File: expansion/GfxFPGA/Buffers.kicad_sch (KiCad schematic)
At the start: 20 parts, among them U201 SN74LVC8T245PWR, U202 SN74LVC8T245PWR, U203 SN74LVC8T245PWR, U204 SN74LVC8T245PWR, U205 SN74LVC8T245PWR, U206 SN74LVC8T245PWR

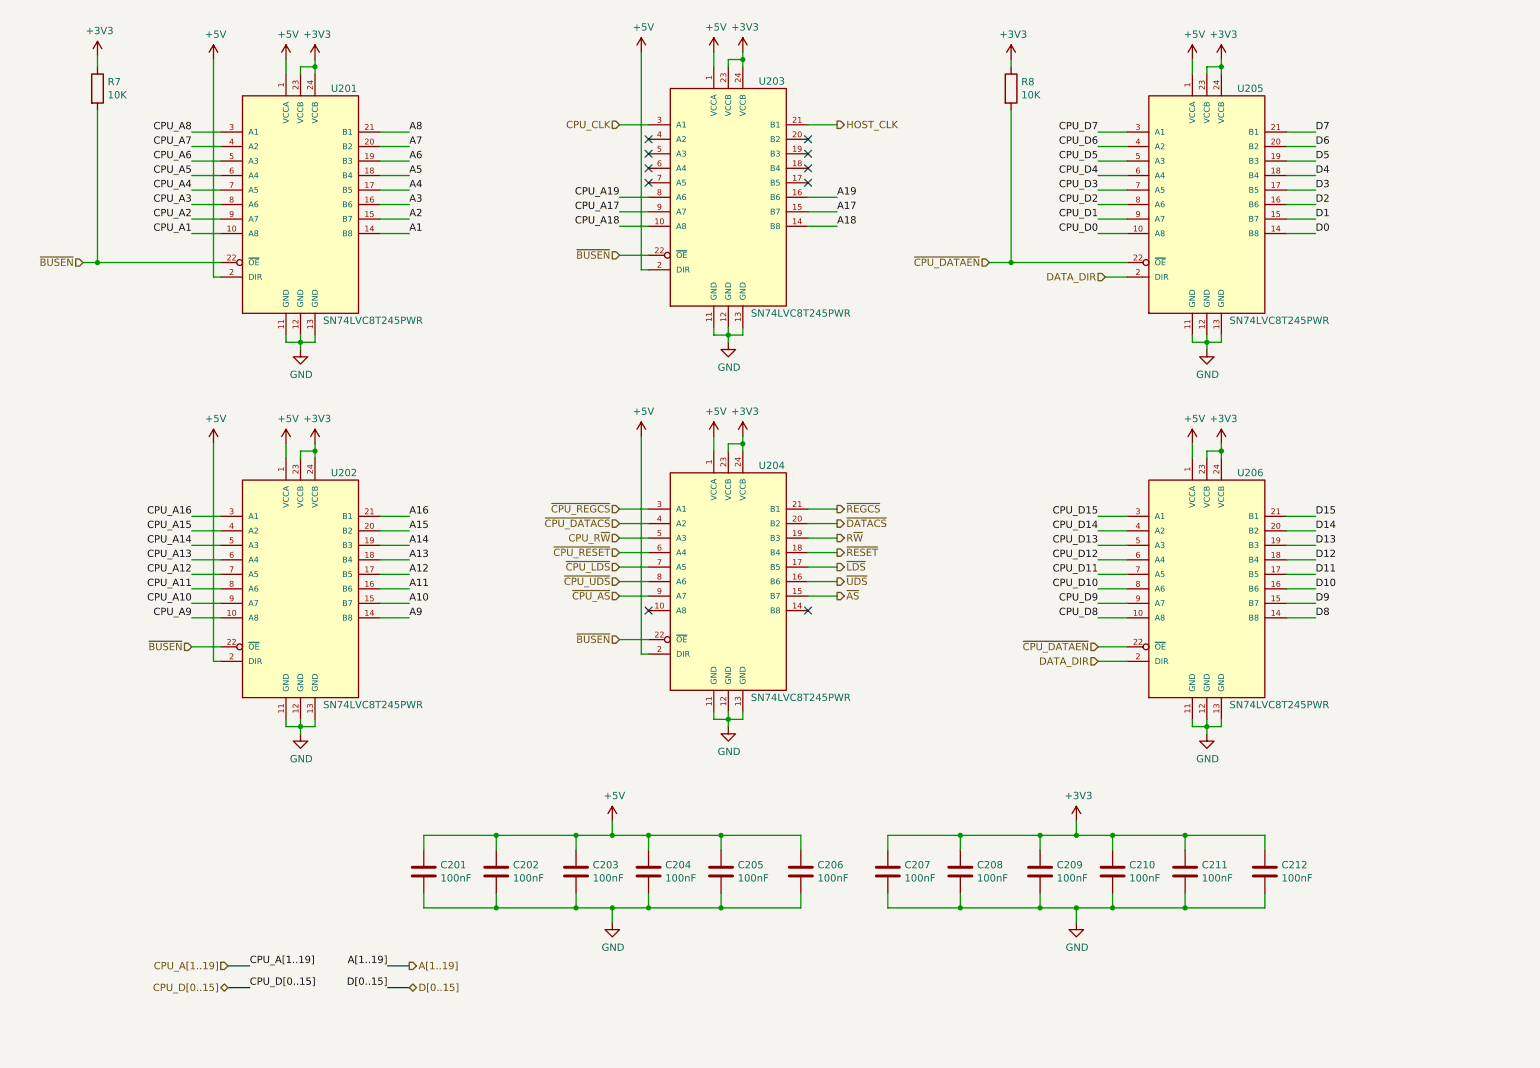
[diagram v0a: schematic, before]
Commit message: WOrking on FPGA VGA board
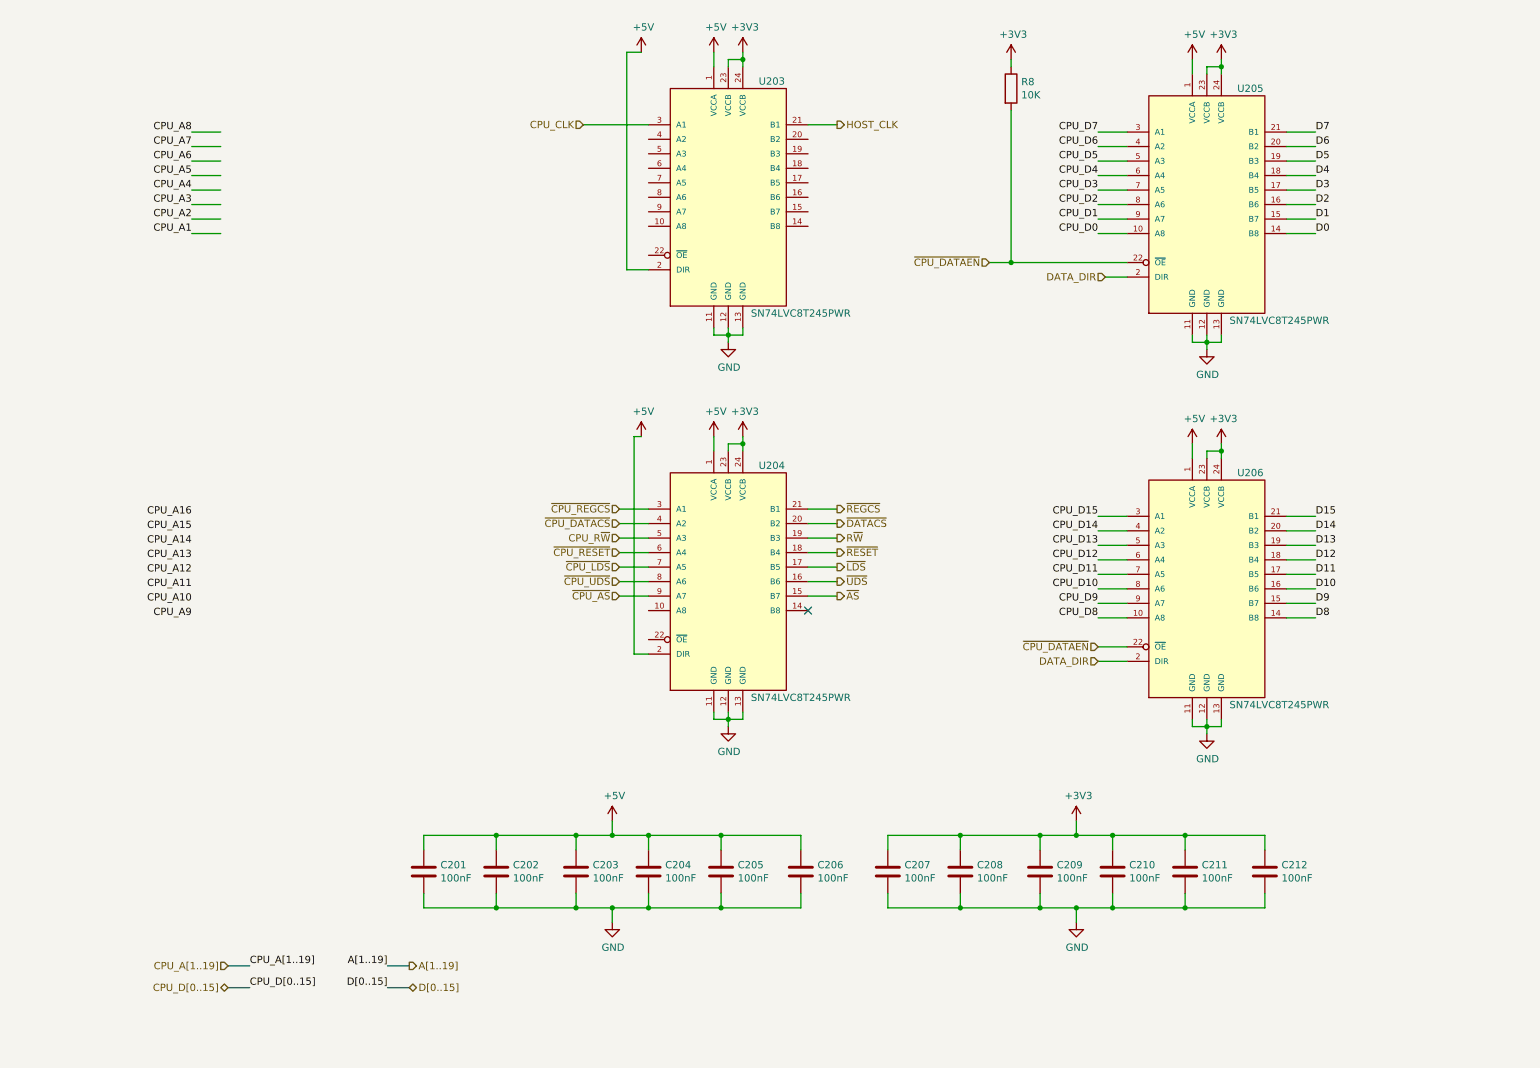
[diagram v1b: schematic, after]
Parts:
- removed R7: 10K, Resistor_SMD:R_0805_2012Metric, symbol Device:R
- removed U201, U202: SN74LVC8T245PWR, Ddraig:SOP65P640X120-24N, symbol Ddraig:SN74LVC8T245PWR
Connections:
- net A17: no longer names the net of U203.15 (B7)
- net A18: no longer names the net of U203.14 (B8)
- net A19: no longer names the net of U203.16 (B6)
- net CPU_A17: no longer names the net of U203.9 (A7)
- net CPU_A18: no longer names the net of U203.10 (A8)
- net CPU_A19: no longer names the net of U203.8 (A6)
- net ~{BUSEN}: no longer names the net of U203.22 (~{OE})
- net ~{BUSEN}: no longer U204.22 (~{OE})
- no-connect marks 10 -> 1

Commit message: WOrking on VGA card
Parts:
- removed C212: 100nF, Capacitor_SMD:C_0805_2012Metric, symbol Device:C
- added C25: 100nF, Capacitor_SMD:C_0805_2012Metric, symbol Device:C
- added U5, U6, U7: SN74LS157NSR, Package_SO:SO-16_5.3x10.2mm_P1.27mm, symbol 74xx:74LS157
- added U8: SN74LV1T34DBV, Package_TO_SOT_SMD:SOT-23-5, symbol Logic_LevelTranslator:SN74LV1T34DBV
- renumbered C208 to C21, C209 to C22, C210 to C23, C211 to C24, C201 to C26, C202 to C27, C203 to C28, C204 to C29, C205 to C30, C206 to C31, C207 to C32, R8 to R20, U204 to U10, U205 to U11, U206 to U12, U203 to U9
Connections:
- net +3V3: now also C25.1, U8.5 (VCC); no longer C32.1
- net +5V: now also C32.1, U5.16 (VCC), U6.16 (VCC), U7.16 (VCC)
- net CPU_A1: now also U5.2 (I0a)
- net CPU_A10: now also U6.5 (I0b)
- net CPU_A11: now also U5.3 (I1a)
- net CPU_A12: now also U5.6 (I1b)
- net CPU_A13: now also U5.10 (I1c)
- net CPU_A14: now also U5.13 (I1d)
- net CPU_A15: now also U7.3 (I1a)
- net CPU_A16: now also U7.6 (I1b)
- net CPU_A2: now also U5.5 (I0b)
- net CPU_A3: now also U5.11 (I0c)
- net CPU_A4: now also U5.14 (I0d)
- net CPU_A5: now also U7.2 (I0a)
- net CPU_A6: now also U7.5 (I0b)
- net CPU_A7: now also U7.11 (I0c)
- net CPU_A8: now also U7.14 (I0d)
- net CPU_A9: now also U6.2 (I0a)
- net CPU_D0: now also U11.3 (A1); no longer U11.10 (A8)
- net CPU_D1: now also U11.4 (A2); no longer U11.9 (A7)
- net CPU_D10: now also U12.5 (A3); no longer U12.8 (A6)
- net CPU_D11: now also U12.6 (A4); no longer U12.7 (A5)
- net CPU_D12: now also U12.7 (A5); no longer U12.6 (A4)
- net CPU_D13: now also U12.8 (A6); no longer U12.5 (A3)
- net CPU_D14: now also U12.9 (A7); no longer U12.4 (A2)
- net CPU_D15: now also U12.10 (A8); no longer U12.3 (A1)
- net CPU_D2: now also U11.5 (A3); no longer U11.8 (A6)
- net CPU_D3: now also U11.6 (A4); no longer U11.7 (A5)
- net CPU_D4: now also U11.7 (A5); no longer U11.6 (A4)
- net CPU_D5: now also U11.8 (A6); no longer U11.5 (A3)
- net CPU_D6: now also U11.9 (A7); no longer U11.4 (A2)
- net CPU_D7: now also U11.10 (A8); no longer U11.3 (A1)
- net CPU_D8: now also U12.3 (A1); no longer U12.10 (A8)
- net CPU_D9: now also U12.4 (A2); no longer U12.9 (A7)
- net D0: now also U11.21 (B1); no longer U11.14 (B8)
- net D1: now also U11.20 (B2); no longer U11.15 (B7)
- net D10: now also U12.19 (B3); no longer U12.16 (B6)
- net D11: now also U12.18 (B4); no longer U12.17 (B5)
- net D12: now also U12.17 (B5); no longer U12.18 (B4)
- net D13: now also U12.16 (B6); no longer U12.19 (B3)
- net D14: now also U12.15 (B7); no longer U12.20 (B2)
- net D15: now also U12.14 (B8); no longer U12.21 (B1)
- net D2: now also U11.19 (B3); no longer U11.16 (B6)
- net D3: now also U11.18 (B4); no longer U11.17 (B5)
- net D4: now also U11.17 (B5); no longer U11.18 (B4)
- net D5: now also U11.16 (B6); no longer U11.19 (B3)
- net D6: now also U11.15 (B7); no longer U11.20 (B2)
- net D7: now also U11.14 (B8); no longer U11.21 (B1)
- net D8: now also U12.21 (B1); no longer U12.14 (B8)
- net D9: now also U12.20 (B2); no longer U12.15 (B7)
- net GND: now also U10.22 (~{OE}), U9.22 (~{OE}), C25.2, U5.15 (E), U5.8 (GND), U6.10 (I1c), U6.11 (I0c), U6.13 (I1d), U6.14 (I0d), U6.15 (E), U6.6 (I1b), U6.8 (GND), U7.15 (E), U7.8 (GND), U8.3 (GND)
- net ~{AS}: now also U8.4 (Y); no longer U10.15 (B7)
- net ~{CPU_AS}: now also U8.2 (A); no longer U10.9 (A7)
- net MUX_A7: now reaches U9.10 (A8)
- net MUX_A7: now also U7.12 (Zd)
- net A7: now reaches U9.14 (B8)
- net A6: now reaches U9.15 (B7)
- net A5: now reaches U9.16 (B6)
- net A4: now reaches U9.17 (B5)
- net A3: now reaches U9.18 (B4)
- net A2: now reaches U9.19 (B3)
- net A1: now reaches U9.20 (B2)
- net MUX_A1: now reaches U9.4 (A2)
- net MUX_A1: now also U5.7 (Zb)
- net MUX_A2: now reaches U9.5 (A3)
- net MUX_A2: now also U5.9 (Zc)
- net MUX_A3: now reaches U9.6 (A4)
- net MUX_A3: now also U5.12 (Zd)
- net MUX_A4: now reaches U9.7 (A5)
- net MUX_A4: now also U7.4 (Za)
- net MUX_A5: now reaches U9.8 (A6)
- net MUX_A5: now also U7.7 (Zb)
- net MUX_A6: now reaches U9.9 (A7)
- net MUX_A6: now also U7.9 (Zc)
- net MUX_A9: now reaches U10.10 (A8)
- net MUX_A9: now also U6.7 (Zb)
- net A9: now reaches U10.14 (B8)
- net CPU_CLK renamed MUX_A0
- net MUX_A0: now also U5.4 (Za)
- net HOST_CLK renamed A0
- new net A8: U10.15 (B7)
- new net ADDR_MUX: U5.1 (S), U6.1 (S), U7.1 (S)
- new net CPU_A17: U7.10 (I1c)
- new net CPU_A18: U7.13 (I1d)
- new net CPU_A19: U6.3 (I1a)
- new net MUX_A8: U10.9 (A7), U6.4 (Za)
- no-connect marks 1 -> 2
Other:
- moved on the sheet: C21, C22, C23, C24, C26, C27, C28, C29, C30, C31, C32, R20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
